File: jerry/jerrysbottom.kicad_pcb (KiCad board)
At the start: 2 copper layers, 95 x 94 mm, 1 part

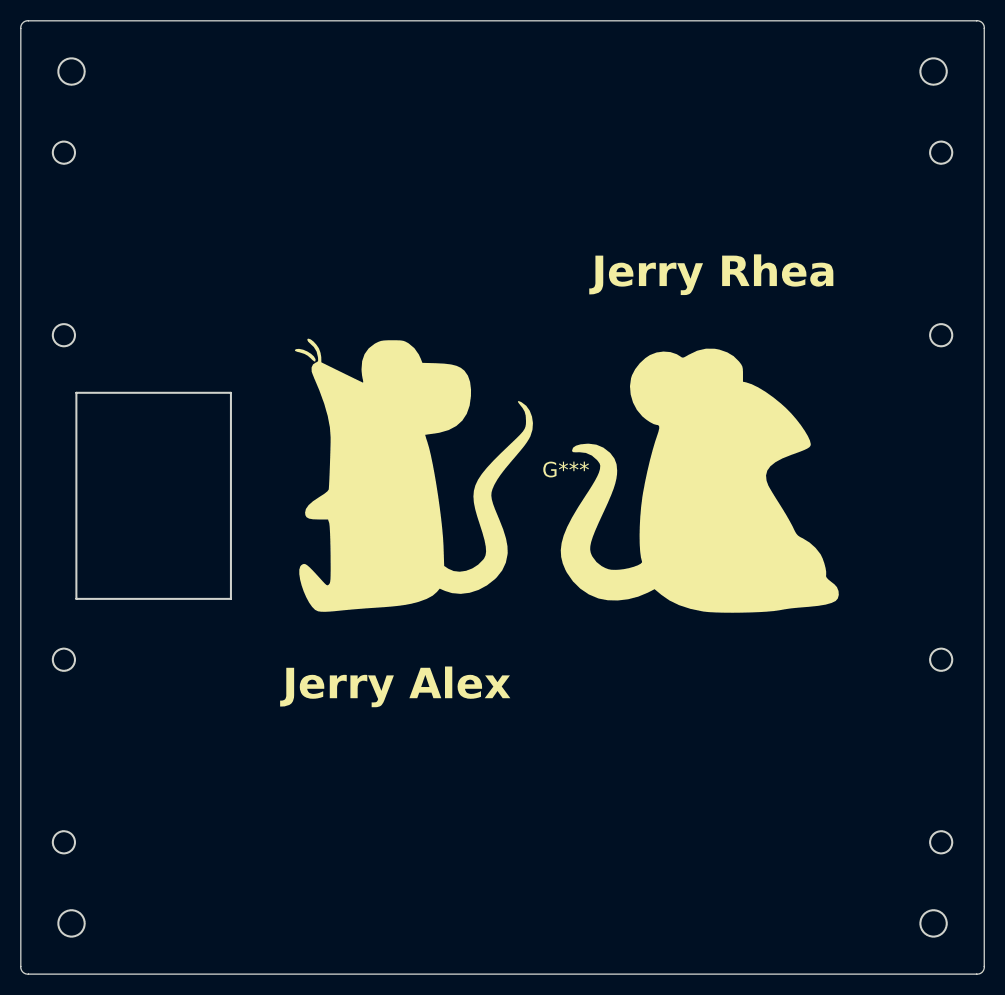
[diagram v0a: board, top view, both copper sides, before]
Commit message: Updated for manufacturing
fixed gerber errors, genereated gerbers
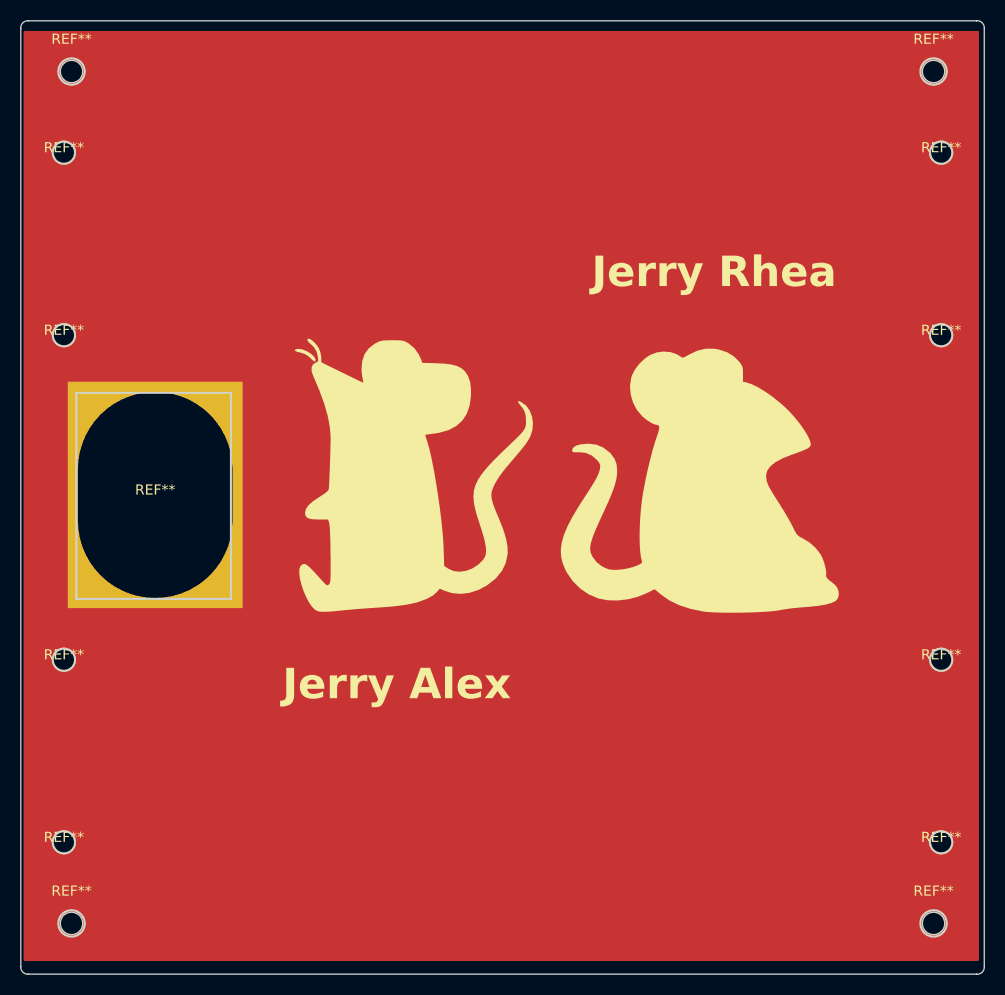
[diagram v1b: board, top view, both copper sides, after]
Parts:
- added REF**: MotorMountCutout, tempjerry:MotorMountCutout, F.Cu at (115.8, 101.0)
- added REF**: MountingHole_2.2mm_M2, MountingHole:MountingHole_2.2mm_M2, F.Cu at (115.0, 75.0)
- added REF**: MotorMountCutout, tempjerry:MotorMountCutout, F.Cu at (115.8, 151.0)
- added REF**: MotorMountCutout, tempjerry:MotorMountCutout, F.Cu at (29.2, 101.0)
- added REF**: MotorMountCutout, tempjerry:MotorMountCutout, F.Cu at (29.2, 83.0)
- added REF**: SquareHole, tempjerry:SquareHole, F.Cu at (38.2, 116.8)
- added REF**: MountingHole_2.2mm_M2, MountingHole:MountingHole_2.2mm_M2, F.Cu at (30.0, 75.0)
- added REF**: MountingHole_2.2mm_M2, MountingHole:MountingHole_2.2mm_M2, F.Cu at (30.0, 159.0)
- added REF**: MotorMountCutout, tempjerry:MotorMountCutout, F.Cu at (115.8, 83.0)
- added REF**: MotorMountCutout, tempjerry:MotorMountCutout, F.Cu at (29.2, 133.0)
- added REF**: MotorMountCutout, tempjerry:MotorMountCutout, F.Cu at (115.8, 133.0)
- added REF**: MotorMountCutout, tempjerry:MotorMountCutout, F.Cu at (29.2, 151.0)
- added REF**: MountingHole_2.2mm_M2, MountingHole:MountingHole_2.2mm_M2, F.Cu at (115.0, 159.0)
